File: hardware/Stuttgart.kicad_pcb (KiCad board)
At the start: 2 copper layers, 100 x 100 mm, 34 parts, among them IC1 NCV1117ST33T3G, J1 USB_C_Receptacle_USB2.0_16P, J2 FCR7350, J3 FCR7350, J4 FCR7350, J5 SM03B-SRSS-TB_LF__SN_, U1 RP2354A, Y1 ABM8-272-T3

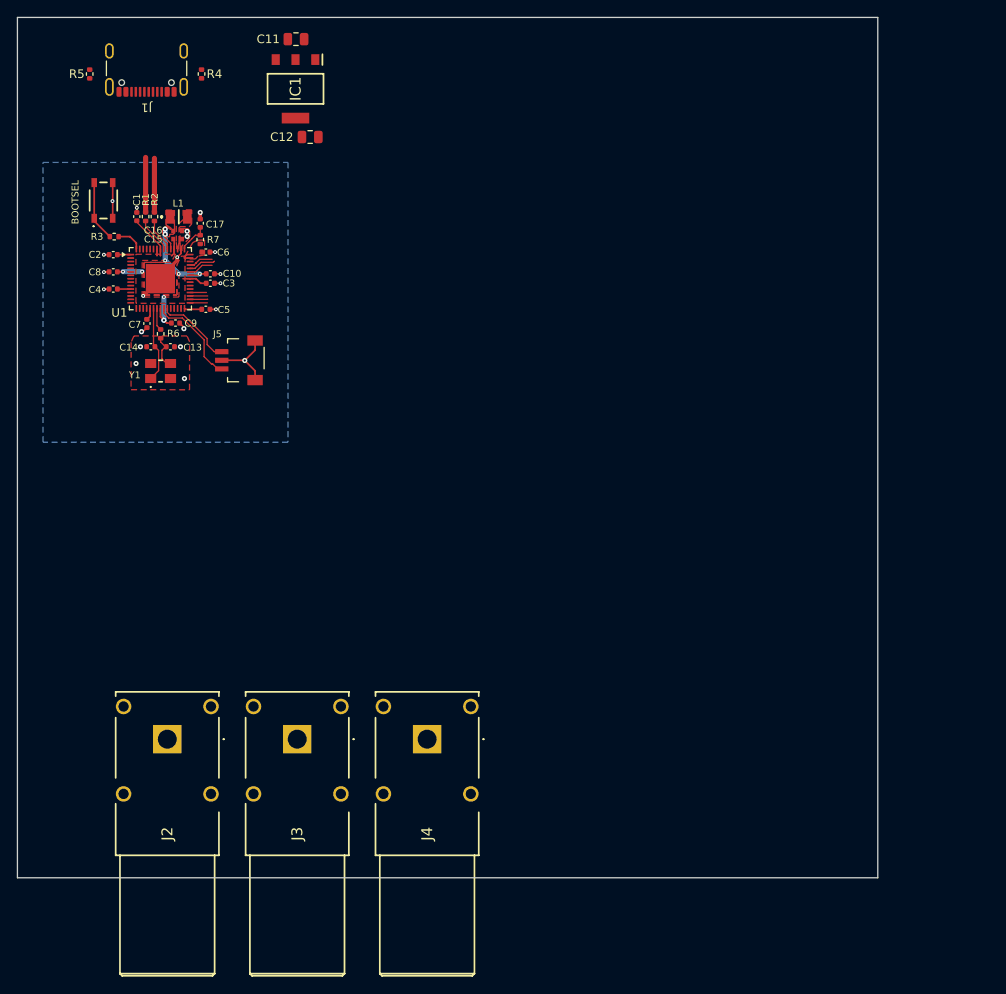
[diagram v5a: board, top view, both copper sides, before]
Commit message: Added DCDC IC
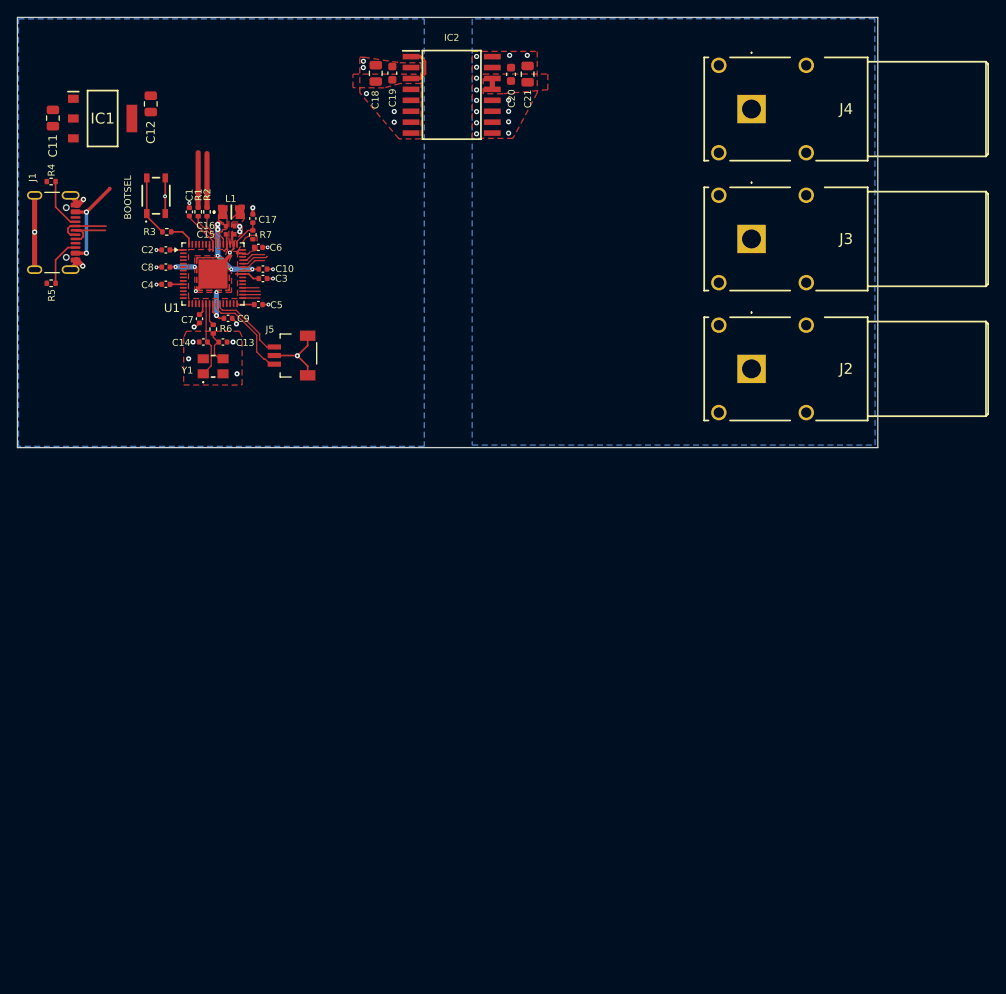
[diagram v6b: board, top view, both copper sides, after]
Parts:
- added C18: 10u, Capacitor_SMD:C_0805_2012Metric, F.Cu at (144.7, 62.0)
- added C19: 100n, Capacitor_SMD:C_0603_1608Metric, F.Cu at (146.6, 62.0)
- added C20: 100n, Capacitor_SMD:C_0603_1608Metric, F.Cu at (160.4, 62.1)
- added C21: 10u, Capacitor_SMD:C_0805_2012Metric, F.Cu at (162.3, 62.1)
- added IC2: UCC12040DVER, Stuttgart:SOIC127P1030X265-16N, F.Cu at (153.5, 64.5)
- moved J4 82.4 mm to (188.3, 66.2), turned to 180 degrees
- moved J2 80.4 mm to (188.3, 96.3), turned to 180 degrees
- moved J3 78.5 mm to (188.3, 81.2), turned to 180 degrees
- moved C11 29.7 mm to (107.1, 67.2), turned to 90 degrees
- moved R5 24.7 mm to (106.9, 86.4), turned to 0 degrees
- moved J1 23.3 mm to (106.1, 80.5), turned to -90 degrees
- moved IC1 22.7 mm to (112.9, 67.2), turned to 0 degrees
- moved R4 21.5 mm to (106.9, 74.6), turned to 0 degrees
- moved C12 18.9 mm to (118.5, 65.5), turned to 90 degrees
- moved J5 6.14 mm to (135.3, 94.8)
- moved C3 6.14 mm to (131.5, 85.8)
- moved L1 6.14 mm to (127.9, 78.1)
- moved R2 6.14 mm to (125.0, 78.1)
- moved C10 6.14 mm to (131.5, 84.8)
- moved C7 6.14 mm to (124.2, 90.5)
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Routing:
- net VBUS: track 0.00 -> 16.3 mm, vias 0 -> 2
- net GND: track 27.3 -> 41.0 mm, vias 21 -> 29
- net Net-(J1-CC1): track 0.00 -> 5.99 mm
- net USB_D-: track 6.27 -> 12.2 mm
- net USB_D+: track 6.36 -> 12.3 mm
- net Net-(J1-CC2): track 0.00 -> 5.63 mm
- net +5V: track 0.00 -> 1.27 mm
- net GND1: vias 0 -> 14
- added copper zone on F.Cu, net +5V
- added copper zone on B.Cu, net GND1
- added copper zone on F.Cu, net GND1
- added copper zone on F.Cu, net VBUS
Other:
- board size 100 x 100 mm -> 100 x 50 mm

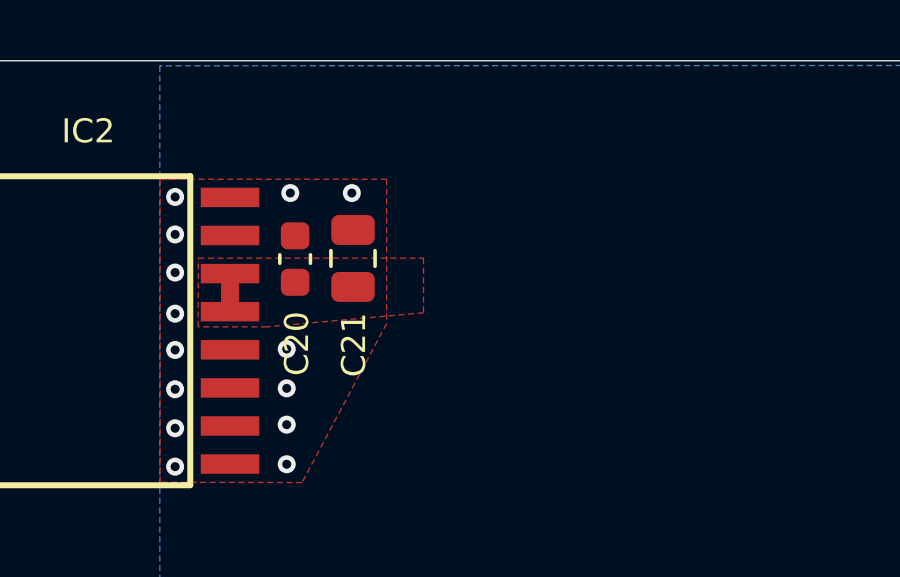
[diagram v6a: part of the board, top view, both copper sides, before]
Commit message: Added 3V3-1 LDO
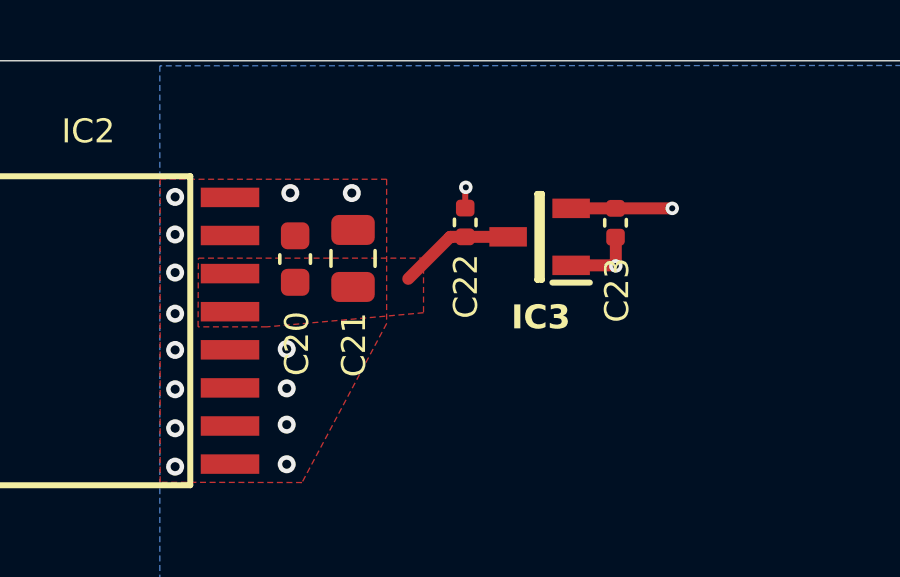
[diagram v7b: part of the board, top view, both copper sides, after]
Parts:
- added C22: 1u, Capacitor_SMD:C_0402_1005Metric, F.Cu at (166.0, 60.9)
- added C23: 1u, Capacitor_SMD:C_0402_1005Metric, F.Cu at (171.1, 60.9)
- added IC3: MCP1700T-3302E_TT, Stuttgart:SOT95P237X112-3N, F.Cu at (168.5, 61.4)
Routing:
- net GND1: track 0.00 -> 3.70 mm, vias 14 -> 16
- net +3.3VA: track 0.00 -> 3.37 mm, vias 0 -> 1
- net +5V: track 1.27 -> 3.91 mm

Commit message: Further ISO bridge development
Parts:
- added C24: 100n, Capacitor_SMD:C_0402_1005Metric, F.Cu at (148.3, 72.5)
- added C25: 100n, Capacitor_SMD:C_0402_1005Metric, F.Cu at (158.4, 72.3)
- added IC4: ISO7742DBQR, Stuttgart:SOP64P600X175-16N, F.Cu at (153.5, 74.6)
